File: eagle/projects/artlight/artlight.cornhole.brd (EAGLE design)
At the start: 58.4 x 58.4 mm, 21 parts, among them T1 2N2222, T2 2N2222, T3 2N2222, T4 2N2222, T5 2N2222, T6 2N2222

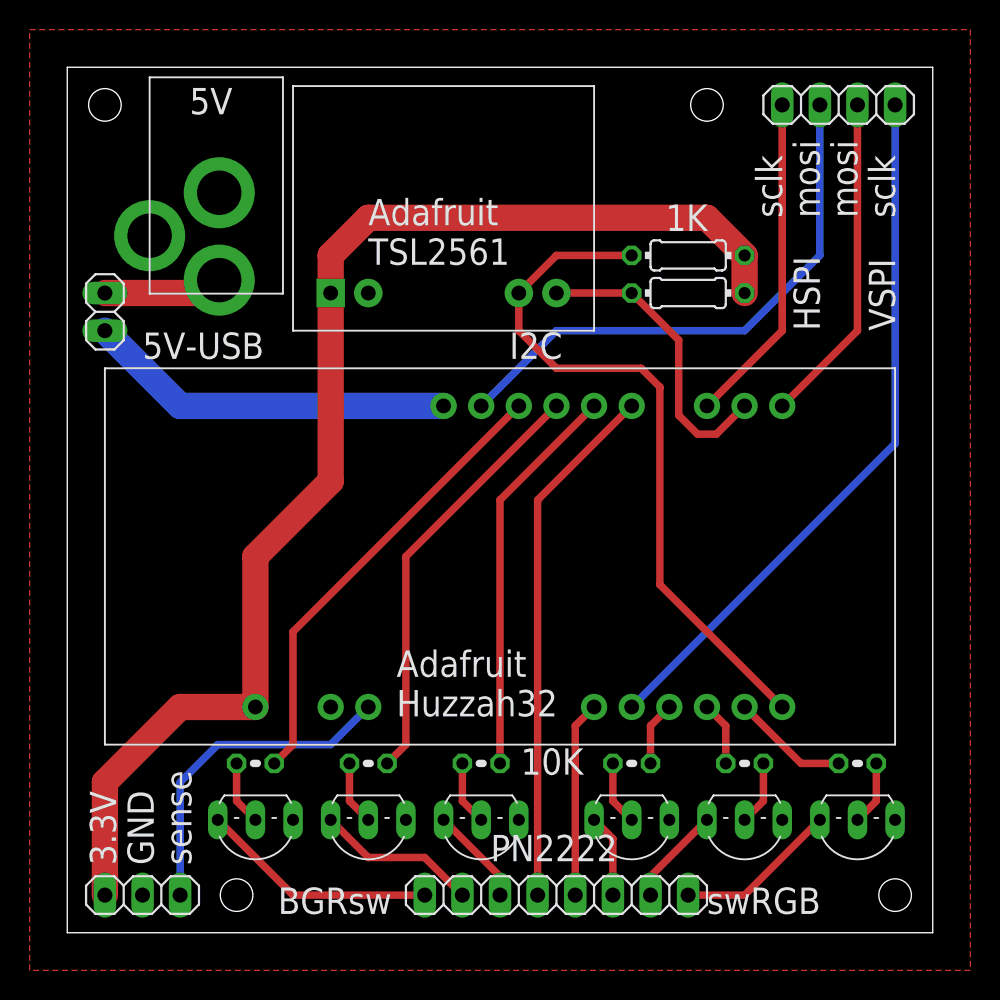
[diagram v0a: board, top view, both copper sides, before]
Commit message: eagle: artlight.cornhole: fix ground pour, add ledsw2
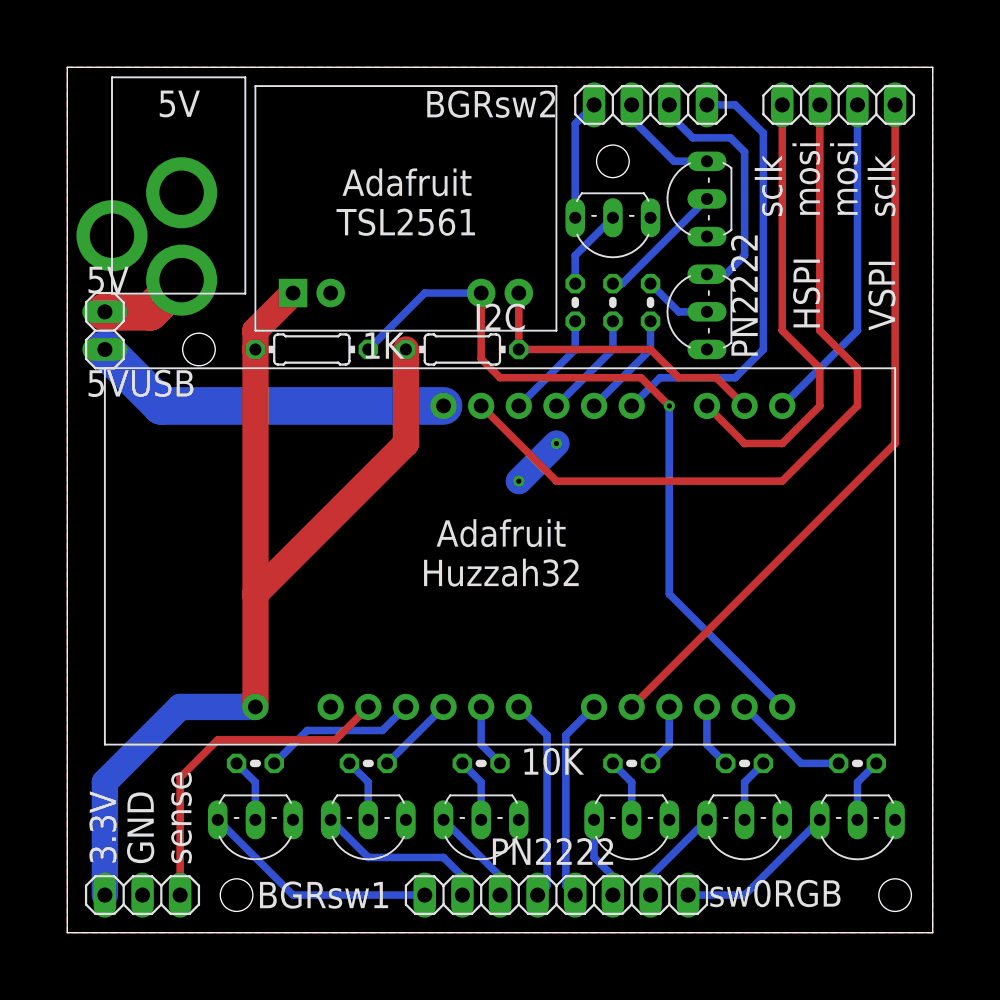
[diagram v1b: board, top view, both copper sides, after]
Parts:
- added JP5: LED-SW-2, pinhead:1X04
- added R10, R11, R9: 10K, rcl:0204V
- added T7, T8, T9: 2N2222, adafruit:TO92-EBC-OVAL
- moved R2 26.2 mm to (16.5, 39.4), turned to 180 degrees
- moved R1 15.7 mm to (26.7, 39.4), turned to 180 degrees
- moved U$2 2.54 mm to (7.62, 53.3)
- moved U$3 2.54 mm to (22.9, 48.3)
- moved JP1 1.27 mm to (2.54, 40.6)
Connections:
- new net LED2B: R9.1, U$1.LED2B
- new net LED2B-BASE: R9.2, T7.B
- new net LED2B-PIN: JP5.1, T7.C
- new net LED2G: R10.1, U$1.LED2G
- new net LED2G-BASE: R10.2, T8.B
- new net LED2G-PIN: JP5.2, T8.C
- new net LED2R: R11.1, U$1.LED2R
- new net LED2R-BASE: R11.2, T9.B
- new net LED2R-PIN: JP5.3, T9.C
- new net SW2: JP5.4, U$1.SW2
- net GND: now also T7.E, T8.E, T9.E
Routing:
- net SW2: track 0.00 -> 29.7 mm
- net LED1G: track 28.9 -> 5.39 mm
- net LED1R: track 26.8 -> 4.34 mm
- net SW1: track 35.7 -> 13.8 mm
- net LED1B: track 31.0 -> 10.5 mm
- net LED2R-PIN: track 0.00 -> 16.8 mm
- net +3V3: track 85.1 -> 69.6 mm
- net HSPI-MOSI: track 37.2 -> 51.0 mm
- net LED2G-BASE: track 0.00 -> 8.72 mm
- net HSPI-SCLK: track 22.4 -> 31.1 mm
- net LED2B-PIN: track 0.00 -> 8.15 mm
- net LED2B: track 0.00 -> 7.29 mm
- net LED2R: track 0.00 -> 7.29 mm
- net LED2G: track 0.00 -> 7.29 mm
- net LED2G-PIN: track 0.00 -> 7.22 mm
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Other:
- board text added: "(BGRsw2) LED Switches (sw1RGB)"
- board text added: "BGRsw1"
- board text added: "BGRsw2"
- board text added: "LED Switch (sw2RGB)"
- board text added: "sw0RGB"
- board text removed: "5V-USB"
- board text removed: "BGRsw"
- board text removed: "LED Switches"
- board text removed: "swRGB"

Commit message: eagle: artlight.cornhole, pins
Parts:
- added R12, R13: 47K, rcl:0204/7
- moved R3 1.27 mm to (52.1, 11.4)
- moved R8 1.27 mm to (14.0, 11.4)
- moved R6 1.27 mm to (29.2, 11.4)
- moved R7 1.27 mm to (21.6, 11.4)
- moved R4 1.27 mm to (44.5, 11.4)
- moved R5 1.27 mm to (39.4, 11.4)
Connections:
- net +3V3: now also R12.2, R13.2
- net SW1: now also R12.1
- net SWBB: now also R13.1
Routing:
- net SWBB: track 22.6 -> 36.5 mm
- net SW1: track 13.8 -> 27.1 mm
- net HSPI-SCLK: track 31.1 -> 22.7 mm, vias 0 -> 1
- net SW2: track 29.7 -> 22.4 mm, vias 0 -> 1
- net HSPI-MOSI: track 51.0 -> 46.8 mm
- net GND: track 3.59 -> 0.00 mm, vias 2 -> 0
- net LED1B: track 10.5 -> 7.03 mm
- net +3V3: track 69.6 -> 72.1 mm
- net LED1G: track 5.39 -> 3.81 mm
- net LED0B-PIN: track 11.0 -> 12.5 mm
- net LED0B: track 7.93 -> 7.03 mm
- net I2C-SDA: track 51.1 -> 51.9 mm, vias 1 -> 0
- net LED1B-PIN: track 16.1 -> 16.8 mm
- net LED0R-BASE: track 4.34 -> 3.81 mm
- net LED0R: track 4.34 -> 3.81 mm
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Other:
- board text added: "LED Switch"
- board text added: "LED Switches"
- board text removed: "(BGRsw2) LED Switches (sw1RGB)"
- board text removed: "LED Switch (sw2RGB)"
